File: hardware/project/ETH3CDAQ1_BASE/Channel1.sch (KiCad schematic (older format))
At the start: 2 parts, among them J401 Conn_02x10_Odd_Even, J402 Conn_02x10_Odd_Even

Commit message: PCB layout
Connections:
- net +15V renamed +18V
- net +15VF renamed +18VF
- net -15V renamed -18V
- net -15VF renamed -18VF
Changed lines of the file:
@@
 Comment4 ""
 $EndDescr
-$Comp
-L ETH3CDAQ1:-15VF #PWR0407
-U 1 1 601F4471
-P 4200 4100
-F 0 "#PWR0407" H 4200 3950 50  0001 C CNN
-F 1 "-15VF" V 4215 4227 50  0000 L CNN
-F 2 "" H 4200 4100 50  0001 C CNN
-F 3 "" H 4200 4100 50  0001 C CNN
-	1    4200 4100
-	0    -1   -1   0
-$EndComp
-$Comp
-L ETH3CDAQ1:+15VF #PWR0412
-U 1 1 601F4FB9
-P 4800 4100
-F 0 "#PWR0412" H 4800 3950 50  0001 C CNN
-F 1 "+15VF" V 4815 4228 50  0000 L CNN
-F 2 "" H 4800 4100 50  0001 C CNN
-F 3 "" H 4800 4100 50  0001 C CNN
-	1    4800 4100
-	0    1    1    0
-$EndComp
 Wire Wire Line
 	4800 4100 4750 4100
@@
 Wire Wire Line
 	7250 4000 7300 4000
-$Comp
-L power:+15V #PWR0424
-U 1 1 60241347
-P 7300 4100
-F 0 "#PWR0424" H 7300 3950 50  0001 C CNN
-F 1 "+15V" V 7315 4228 50  0000 L CNN
-F 2 "" H 7300 4100 50  0001 C CNN
-F 3 "" H 7300 4100 50  0001 C CNN
-	1    7300 4100
-	0    1    1    0
-$EndComp
-$Comp
-L power:-15V #PWR0419
-U 1 1 60243962
-P 6700 4100
-F 0 "#PWR0419" H 6700 4200 50  0001 C CNN
-F 1 "-15V" V 6715 4228 50  0000 L CNN
-F 2 "" H 6700 4100 50  0001 C CNN
-F 3 "" H 6700 4100 50  0001 C CNN
-	1    6700 4100
-	0    -1   -1   0
-$EndComp
 Wire Wire Line
 	4250 3700 3550 3700
@@
 	0    -1   -1   0
 $EndComp
+$Comp
+L ETH3CDAQ1:-18VF #PWR0407
+U 1 1 5FB6846E
+P 4200 4100
+F 0 "#PWR0407" H 4200 3950 50  0001 C CNN
+F 1 "-18VF" V 4200 4250 50  0000 L CNN
+F 2 "" H 4200 4100 50  0001 C CNN
+F 3 "" H 4200 4100 50  0001 C CNN
+	1    4200 4100
+	0    -1   -1   0
+$EndComp
+$Comp
+L ETH3CDAQ1:+18VF #PWR0412
+U 1 1 5FB6CF53
+P 4800 4100
+F 0 "#PWR0412" H 4800 3950 50  0001 C CNN
+F 1 "+18VF" V 4800 4250 50  0000 L CNN
+F 2 "" H 4800 4100 50  0001 C CNN
+F 3 "" H 4800 4100 50  0001 C CNN
+	1    4800 4100
+	0    1    1    0
+$EndComp
+$Comp
+L ETH3CDAQ1:-18V #PWR0101
+U 1 1 6002B31D
+P 6700 4100
+F 0 "#PWR0101" H 6700 3950 50  0001 C CNN
+F 1 "-18V" V 6700 4250 50  0000 L CNN
+F 2 "" H 6700 4100 50  0001 C CNN
+F 3 "" H 6700 4100 50  0001 C CNN
+	1    6700 4100
+	0    -1   -1   0
+$EndComp
+$Comp
+L ETH3CDAQ1:+18V #PWR0102
+U 1 1 6002B800
+P 7300 4100
+F 0 "#PWR0102" H 7300 3950 50  0001 C CNN
+F 1 "+18V" V 7300 4250 50  0000 L CNN
+F 2 "" H 7300 4100 50  0001 C CNN
+F 3 "" H 7300 4100 50  0001 C CNN
+	1    7300 4100
+	0    1    1    0
+$EndComp
 $EndSCHEMATC

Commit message: PCB layout
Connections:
- net +3V3: no longer J402.1 (Pin_1), J402.3 (Pin_3)
- net GND: now also J402.1 (Pin_1), J402.3 (Pin_3)
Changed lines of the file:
@@
 Wire Wire Line
 	4800 3900 4750 3900
-$Comp
-L power:+3.3V #PWR0414
-U 1 1 60232883
-P 6700 3300
-F 0 "#PWR0414" H 6700 3150 50  0001 C CNN
-F 1 "+3.3V" V 6700 3450 50  0000 L CNN
-F 2 "" H 6700 3300 50  0001 C CNN
-F 3 "" H 6700 3300 50  0001 C CNN
-	1    6700 3300
-	0    -1   -1   0
-$EndComp
-$Comp
-L power:+3.3V #PWR0413
-U 1 1 6021ADCA
-P 6700 3200
-F 0 "#PWR0413" H 6700 3050 50  0001 C CNN
-F 1 "+3.3V" V 6700 3350 50  0000 L CNN
-F 2 "" H 6700 3200 50  0001 C CNN
-F 3 "" H 6700 3200 50  0001 C CNN
-	1    6700 3200
-	0    -1   -1   0
-$EndComp
 Wire Wire Line
 	6700 3900 6750 3900
@@
 	0    1    1    0
 $EndComp
+$Comp
+L power:GND #PWR?
+U 1 1 5FCDA1BA
+P 6700 3300
+F 0 "#PWR?" H 6700 3050 50  0001 C CNN
+F 1 "GND" V 6705 3172 50  0000 R CNN
+F 2 "" H 6700 3300 50  0001 C CNN
+F 3 "" H 6700 3300 50  0001 C CNN
+	1    6700 3300
+	0    1    1    0
+$EndComp
+$Comp
+L power:GND #PWR?
+U 1 1 5FCDA55B
+P 6700 3200
+F 0 "#PWR?" H 6700 2950 50  0001 C CNN
+F 1 "GND" V 6705 3072 50  0000 R CNN
+F 2 "" H 6700 3200 50  0001 C CNN
+F 3 "" H 6700 3200 50  0001 C CNN
+	1    6700 3200
+	0    1    1    0
+$EndComp

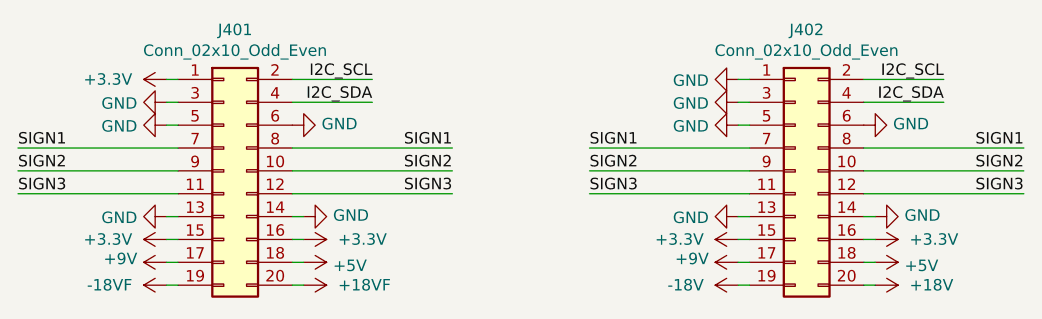
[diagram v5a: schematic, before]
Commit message: Voltage front-end development
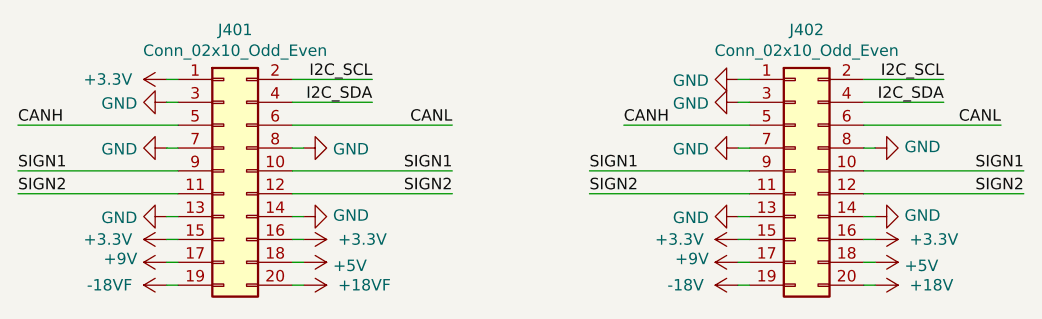
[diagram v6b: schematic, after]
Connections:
- net SIGN3 is gone; now on net SIGN2: J401.11 (Pin_11), J401.12 (Pin_12), J402.11 (Pin_11), J402.12 (Pin_12)
- net GND: now also J401.7 (Pin_7), J401.8 (Pin_8), J402.7 (Pin_7), J402.8 (Pin_8); no longer J401.5 (Pin_5), J401.6 (Pin_6), J402.5 (Pin_5), J402.6 (Pin_6)
- net SIGN1: now also J401.10 (Pin_10), J401.9 (Pin_9), J402.10 (Pin_10), J402.9 (Pin_9); no longer J401.7 (Pin_7), J401.8 (Pin_8), J402.7 (Pin_7), J402.8 (Pin_8)
- net SIGN2: no longer J401.10 (Pin_10), J401.9 (Pin_9), J402.10 (Pin_10), J402.9 (Pin_9)
- new net CANH: J401.5 (Pin_5), J402.5 (Pin_5)
- new net CANL: J401.6 (Pin_6), J402.6 (Pin_6)
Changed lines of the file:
@@
-	0    1    1    0
-$EndComp
-$Comp
-L power:GND #PWR0403
-U 1 1 6020EBB4
-P 4200 3400
-F 0 "#PWR0403" H 4200 3150 50  0001 C CNN
-F 1 "GND" V 4205 3272 50  0000 R CNN
-F 2 "" H 4200 3400 50  0001 C CNN
-F 3 "" H 4200 3400 50  0001 C CNN
-	1    4200 3400
 	0    1    1    0
 $EndComp
@@
 	4250 3600 3550 3600
 Text Label 3550 3600 0    50   ~ 0
-SIGN2
+SIGN1
 Wire Wire Line
 	7250 3200 7600 3200
@@
 	4800 3800 4750 3800
 Wire Wire Line
-	4250 3400 4200 3400
-Wire Wire Line
 	4200 3300 4250 3300
 Wire Wire Line
@@
 Wire Wire Line
 	6750 3300 6700 3300
-Wire Wire Line
-	6700 3400 6750 3400
 $Comp
 L power:+3.3V #PWR0422
@@
 	4250 3700 3550 3700
 Text Label 3550 3700 0    50   ~ 0
-SIGN3
+SIGN2
 Wire Wire Line
 	6700 3800 6750 3800
 Wire Wire Line
 	7250 3800 7300 3800
-Wire Wire Line
-	4250 3500 3550 3500
-Text Label 3550 3500 0    50   ~ 0
-SIGN1
-$Comp
-L power:GND #PWR0408
-U 1 1 60265AB3
-P 4750 3400
-F 0 "#PWR0408" H 4750 3150 50  0001 C CNN
-F 1 "GND" V 4755 3272 50  0000 R CNN
-F 2 "" H 4750 3400 50  0001 C CNN
-F 3 "" H 4750 3400 50  0001 C CNN
-	1    4750 3400
-	0    -1   -1   0
-$EndComp
-$Comp
-L power:GND #PWR0415
-U 1 1 6026BA5F
-P 6700 3400
-F 0 "#PWR0415" H 6700 3150 50  0001 C CNN
-F 1 "GND" V 6705 3272 50  0000 R CNN
-F 2 "" H 6700 3400 50  0001 C CNN
-F 3 "" H 6700 3400 50  0001 C CNN
-	1    6700 3400
-	0    1    1    0
-$EndComp
-$Comp
-L power:GND #PWR0420
-U 1 1 6026C192
-P 7250 3400
-F 0 "#PWR0420" H 7250 3150 50  0001 C CNN
-F 1 "GND" V 7255 3272 50  0000 R CNN
-F 2 "" H 7250 3400 50  0001 C CNN
-F 3 "" H 7250 3400 50  0001 C CNN
-	1    7250 3400
-	0    -1   -1   0
-$EndComp
 Wire Wire Line
 	4750 3600 5450 3600
 Text Label 5450 3600 2    50   ~ 0
-SIGN2
+SIGN1
 Wire Wire Line
 	4750 3700 5450 3700
 Text Label 5450 3700 2    50   ~ 0
-SIGN3
-Wire Wire Line
-	4750 3500 5450 3500
-Text Label 5450 3500 2    50   ~ 0
-SIGN1
+SIGN2
 Wire Wire Line
 	6750 3600 6050 3600
 Text Label 6050 3600 0    50   ~ 0
-SIGN2
+SIGN1
 Wire Wire Line
 	6750 3700 6050 3700
 Text Label 6050 3700 0    50   ~ 0
-SIGN3
-Wire Wire Line
-	6750 3500 6050 3500
-Text Label 6050 3500 0    50   ~ 0
-SIGN1
+SIGN2
 Wire Wire Line
 	7250 3600 7950 3600
 Text Label 7950 3600 2    50   ~ 0
-SIGN2
+SIGN1
 Wire Wire Line
 	7250 3700 7950 3700
 Text Label 7950 3700 2    50   ~ 0
-SIGN3
-Wire Wire Line
-	7250 3500 7950 3500
-Text Label 7950 3500 2    50   ~ 0
-SIGN1
+SIGN2
 $Comp
 L power:+3.3V #PWR0410
@@
 	0    1    1    0
 $EndComp
+Wire Wire Line
+	7250 3400 7850 3400
+Text Label 7850 3400 2    50   ~ 0
+CANL
+Wire Wire Line
+	6750 3400 6200 3400
+Text Label 6200 3400 0    50   ~ 0
+CANH
+$Comp
+L power:GND #PWR0415
+U 1 1 5FCD108A
+P 6700 3500
+F 0 "#PWR0415" H 6700 3250 50  0001 C CNN
+F 1 "GND" V 6705 3372 50  0000 R CNN
+F 2 "" H 6700 3500 50  0001 C CNN
+F 3 "" H 6700 3500 50  0001 C CNN
+	1    6700 3500
+	0    1    1    0
+$EndComp
+Wire Wire Line
+	6700 3500 6750 3500
+$Comp
+L power:GND #PWR0419
+U 1 1 5FCD22C9
+P 7300 3500
+F 0 "#PWR0419" H 7300 3250 50  0001 C CNN
+F 1 "GND" V 7305 3372 50  0000 R CNN
+F 2 "" H 7300 3500 50  0001 C CNN
+F 3 "" H 7300 3500 50  0001 C CNN
+	1    7300 3500
+	0    -1   -1   0
+$EndComp
+Wire Wire Line
+	7300 3500 7250 3500
+$Comp
+L power:GND #PWR0403
+U 1 1 5FCD8663
+P 4200 3500
+F 0 "#PWR0403" H 4200 3250 50  0001 C CNN
+F 1 "GND" V 4205 3372 50  0000 R CNN
+F 2 "" H 4200 3500 50  0001 C CNN
+F 3 "" H 4200 3500 50  0001 C CNN
+	1    4200 3500
+	0    1    1    0
+$EndComp
+Wire Wire Line
+	4200 3500 4250 3500
+$Comp
+L power:GND #PWR0408
+U 1 1 5FCDAA5D
+P 4800 3500
+F 0 "#PWR0408" H 4800 3250 50  0001 C CNN
+F 1 "GND" V 4805 3372 50  0000 R CNN
+F 2 "" H 4800 3500 50  0001 C CNN
+F 3 "" H 4800 3500 50  0001 C CNN
+	1    4800 3500
+	0    -1   1    0
+$EndComp
+Wire Wire Line
+	4800 3500 4750 3500
+Wire Wire Line
+	4250 3400 3550 3400
+Text Label 3550 3400 0    50   ~ 0
+CANH
+Wire Wire Line
+	4750 3400 5450 3400
+Text Label 5450 3400 2    50   ~ 0
+CANL
 $EndSCHEMATC

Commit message: Added selftest circuit in the base PCB.
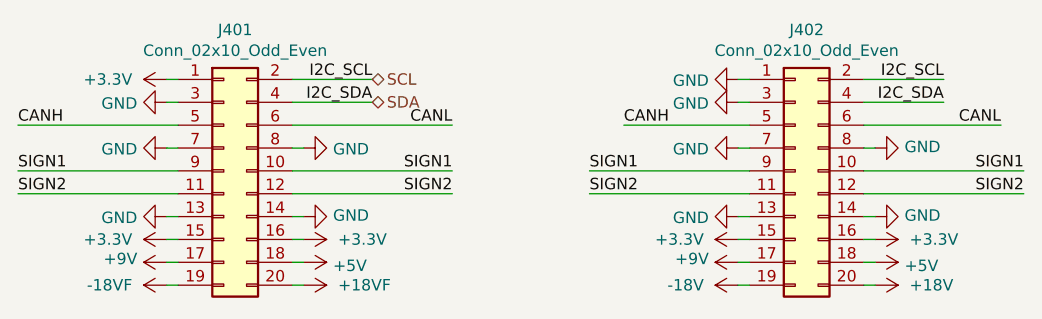
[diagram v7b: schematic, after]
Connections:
- net I2C_SCL renamed SCL
- net I2C_SDA renamed SDA
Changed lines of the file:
@@
 $Descr A4 11693 8268
 encoding utf-8
-Sheet 4 6
+Sheet 4 7
 Title ""
 Date ""
@@
 $EndComp
 $Comp
-L ETH3CDAQ1:-18V #PWR0101
+L ETH3CDAQ1:-18V #PWR0419
 U 1 1 6002B31D
 P 6700 4100
-F 0 "#PWR0101" H 6700 3950 50  0001 C CNN
+F 0 "#PWR0419" H 6700 3950 50  0001 C CNN
 F 1 "-18V" V 6700 4250 50  0000 L CNN
 F 2 "" H 6700 4100 50  0001 C CNN
@@
 $EndComp
 $Comp
-L ETH3CDAQ1:+18V #PWR0102
+L ETH3CDAQ1:+18V #PWR0424
 U 1 1 6002B800
 P 7300 4100
-F 0 "#PWR0102" H 7300 3950 50  0001 C CNN
+F 0 "#PWR0424" H 7300 3950 50  0001 C CNN
 F 1 "+18V" V 7300 4250 50  0000 L CNN
 F 2 "" H 7300 4100 50  0001 C CNN
@@
 	6700 3500 6750 3500
 $Comp
-L power:GND #PWR0419
+L power:GND #PWR0420
 U 1 1 5FCD22C9
 P 7300 3500
-F 0 "#PWR0419" H 7300 3250 50  0001 C CNN
+F 0 "#PWR0420" H 7300 3250 50  0001 C CNN
 F 1 "GND" V 7305 3372 50  0000 R CNN
 F 2 "" H 7300 3500 50  0001 C CNN
@@
 Text Label 5450 3400 2    50   ~ 0
 CANL
+Text HLabel 5100 3200 2    50   BiDi ~ 0
+SCL
+Text HLabel 5100 3300 2    50   BiDi ~ 0
+SDA
 $EndSCHEMATC
